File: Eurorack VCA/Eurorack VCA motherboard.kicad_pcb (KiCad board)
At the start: 2 copper layers, 39 x 100 mm, 23 parts, among them J1 JACK_MONO_SW, J2 JACK_MONO_SW, J3 JACK_MONO_SW, J4 JACK_MONO_SW, J5 JACK_MONO_SW, J6 JACK_MONO_SW, P1 50K, P2 50K, P3 50K, P4 50K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

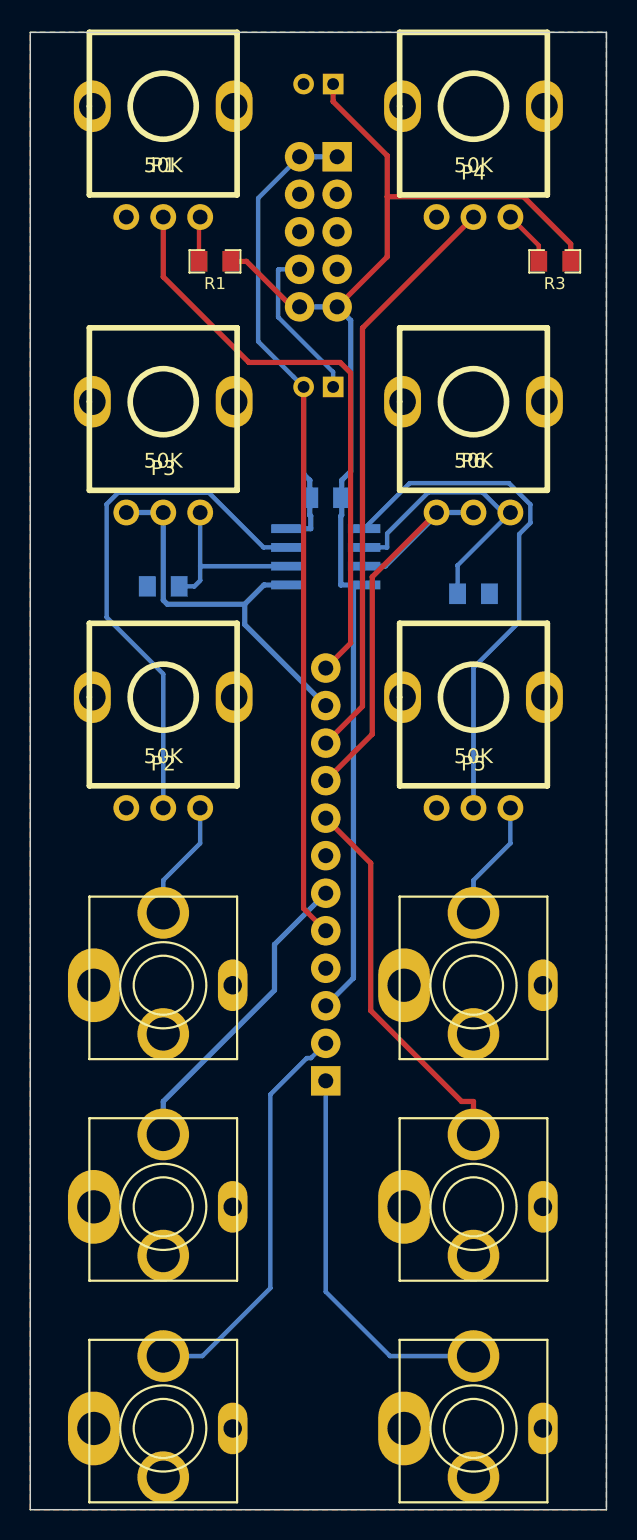
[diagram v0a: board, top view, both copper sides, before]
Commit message: fixed Eurorack VCA CV gain pot. Was reversed. Now v1.1. Ordered updated PCBs from DirtyPCBs.com
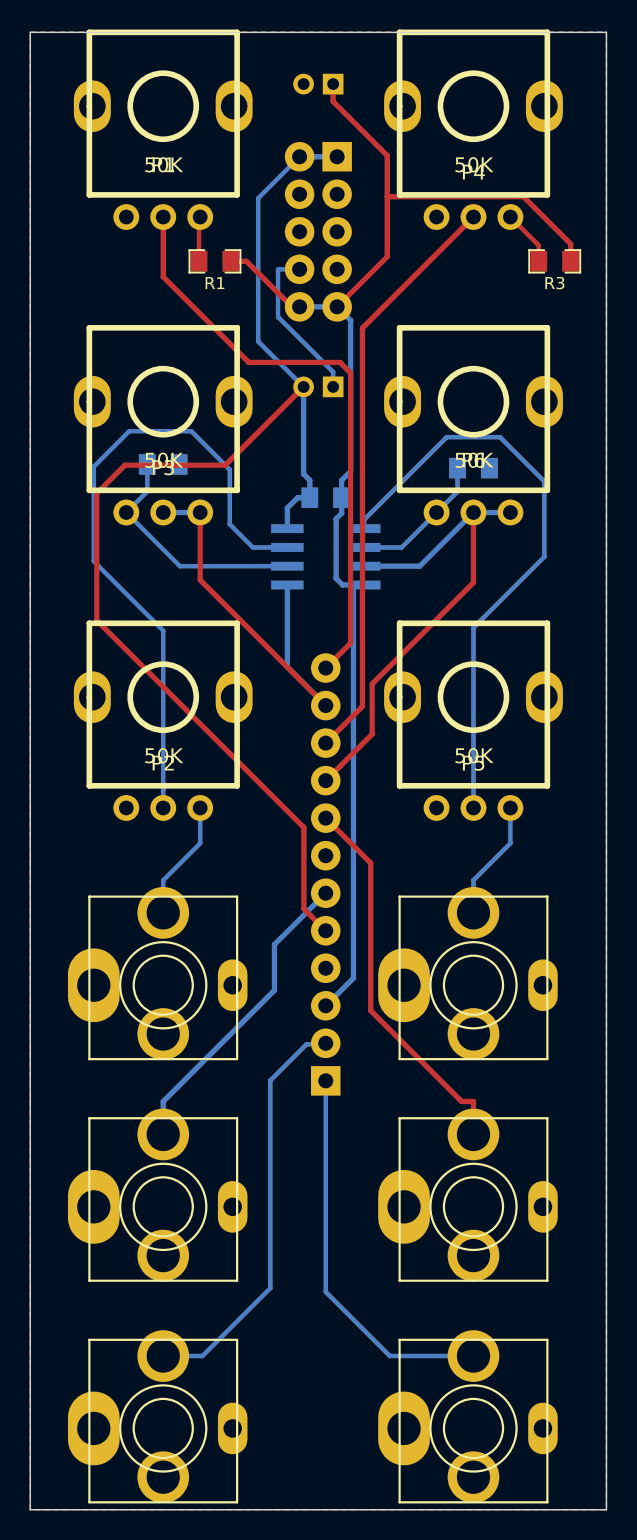
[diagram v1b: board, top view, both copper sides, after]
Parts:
- moved R4 8.50 mm to (234.0, 136.5)
- moved R2 8.25 mm to (213.0, 136.2), turned to 180 degrees
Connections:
- J1 pad 2: (no net) -> Net-(J1-Pad2)
- J2 pad 2: (no net) -> Net-(J2-Pad2)
- J3 pad 2: (no net) -> Net-(J3-Pad2)
- J4 pad 2: (no net) -> Net-(J4-Pad2)
- J5 pad 2: (no net) -> Net-(J5-Pad2)
- J6 pad 2: (no net) -> Net-(J6-Pad2)
- P3 pad 1: CV1A -> Net-(P3-Pad1)
- P3 pad 3: N-0000017 -> CV1A
- P6 pad 1: CV2A -> Net-(P6-Pad1)
- P6 pad 3: N-0000016 -> CV2A
- R2 pad 2: N-0000017 -> Net-(P3-Pad1)
- R4 pad 2: N-0000016 -> Net-(P6-Pad1)
- U1 pad 2: N-0000017 -> Net-(P3-Pad1)
- U1 pad 6: N-0000016 -> Net-(P6-Pad1)
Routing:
- net N-0000016: track 19.4 -> 0.00 mm
- net Net-(P3-Pad1): track 0.00 -> 16.8 mm
- net -12V: track 69.4 -> 84.4 mm
- net N-0000017: track 12.1 -> 0.00 mm
- net Net-(P6-Pad1): track 0.00 -> 9.73 mm
- net Net-(P2-Pad2): track 36.2 -> 44.6 mm
- net Net-(P5-Pad2): track 35.3 -> 40.5 mm
- net CV2A: track 30.3 -> 34.1 mm
- net CV1A: track 26.6 -> 28.4 mm
- net +12V: track 91.7 -> 92.6 mm
- net OUT1: track 27.6 -> 28.2 mm
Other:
- board text added: "v1.1 04 2015"
- board text removed: "v1.0 05 2014"
